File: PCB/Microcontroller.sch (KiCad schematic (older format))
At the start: 25 parts

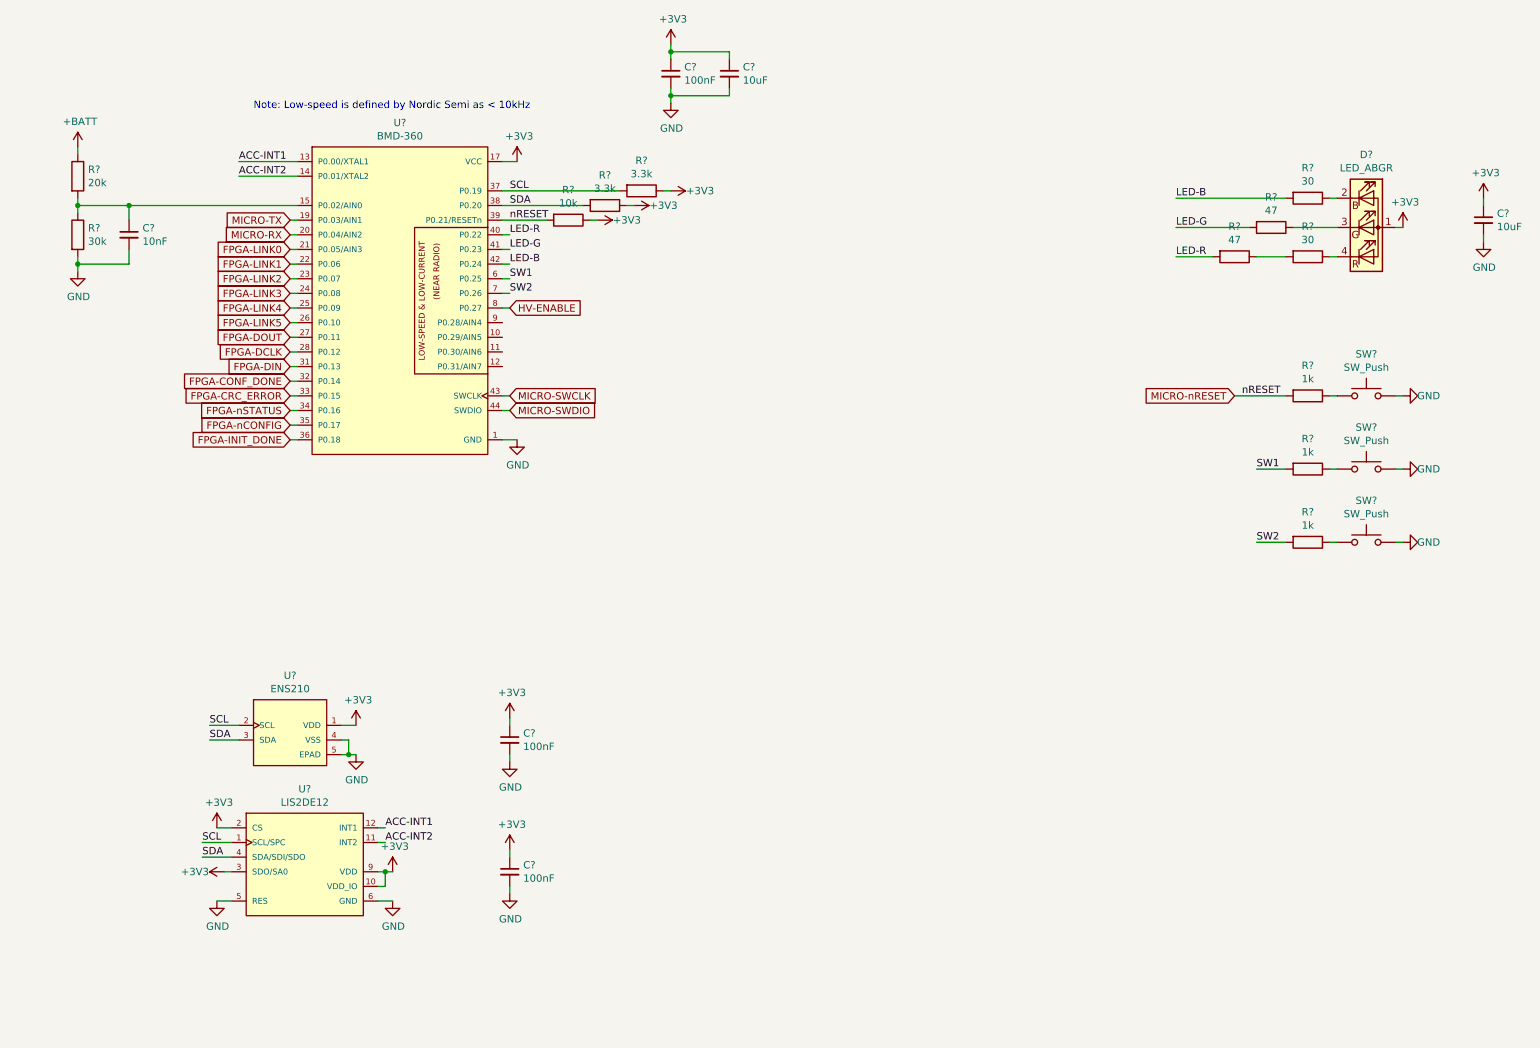
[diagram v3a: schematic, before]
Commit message: Add comparator to monitor 50V supply, add flash memory for storing FPGA config data
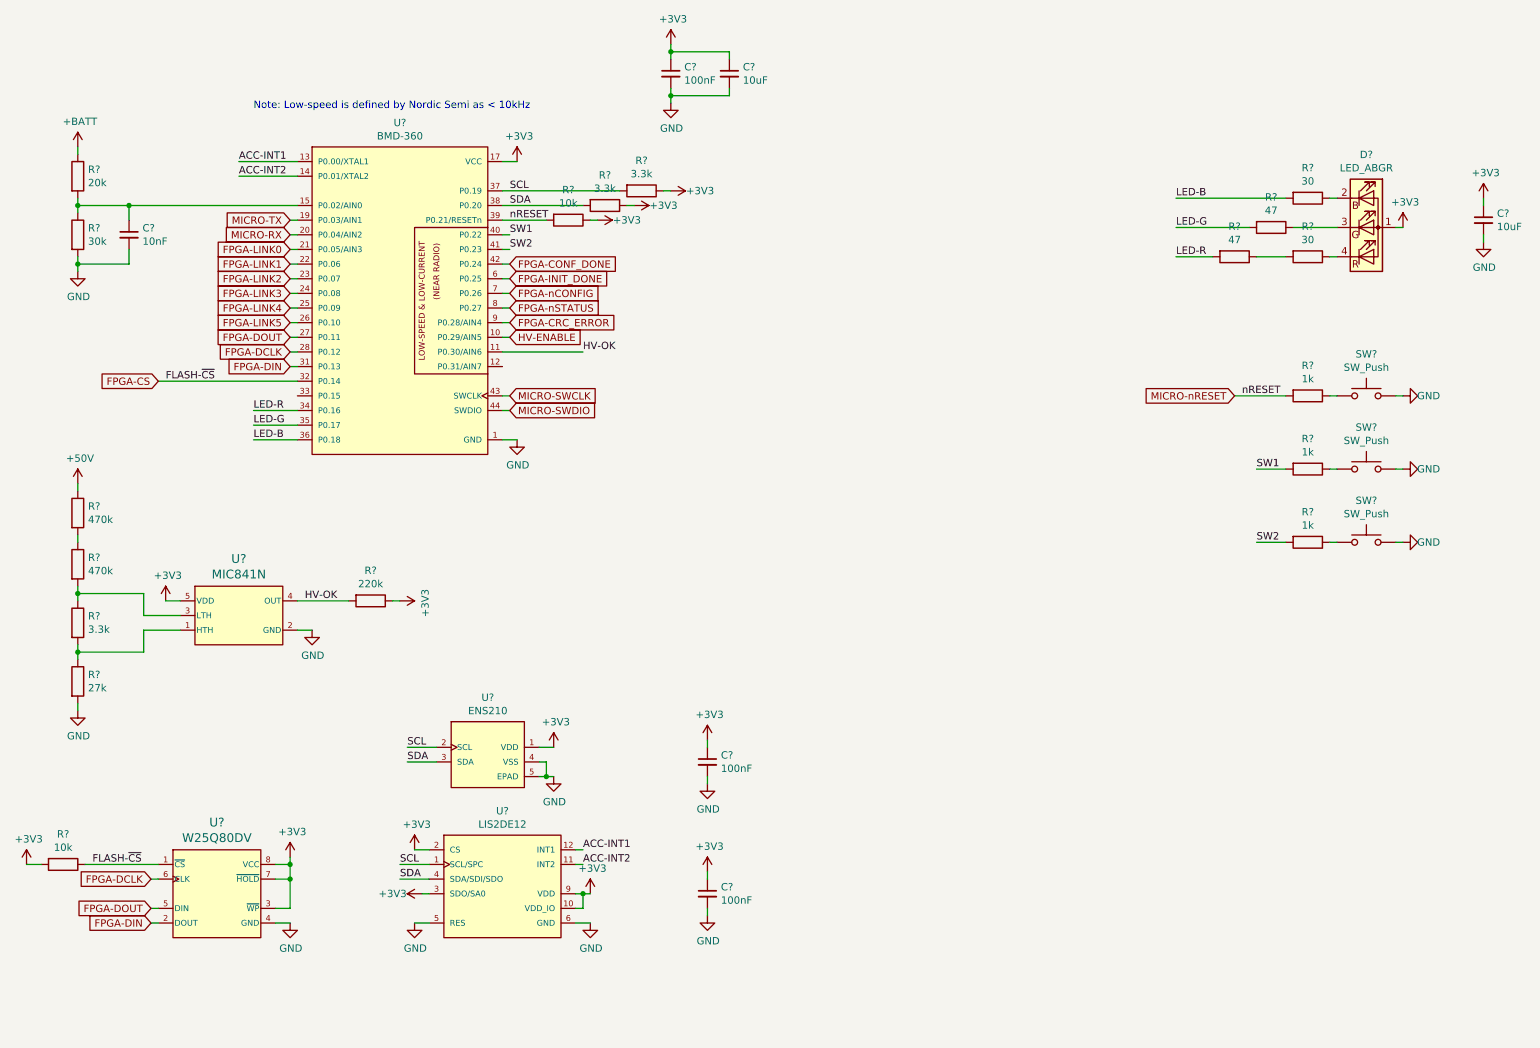
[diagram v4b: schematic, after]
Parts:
- added R?: 3.3k, Resistors_SMD:R_0603_HandSoldering, symbol Device:R
- added R?: 27k, Resistors_SMD:R_0603_HandSoldering, symbol Device:R
- added R? (x2): 470k, Resistors_SMD:R_0603_HandSoldering, symbol Device:R
- added R?: 220k, Resistors_SMD:R_0603_HandSoldering, symbol Device:R
- added R?: 10k, Resistors_SMD:R_0603_HandSoldering, symbol Device:R
- added U?: MIC841N, Parts:SOT353, symbol Parts:MIC841N
- added U?: W25Q80DV, Parts:SOIC8, symbol Parts:W25Q80DV
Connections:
- net +3V3: now also R?.1, R?.2, U?.3 (~WP), U?.5 (VDD), U?.7 (~HOLD), U?.8 (VCC)
- net FPGA-CONF_DONE: now also U?.42 (P0.24); no longer U?.32 (P0.14)
- net FPGA-CRC_ERROR: now also U?.9 (P0.28/AIN4); no longer U?.33 (P0.15)
- net FPGA-DCLK: now also U?.6 (CLK)
- net FPGA-DIN: now also U?.2 (DOUT)
- net FPGA-DOUT: now also U?.5 (DIN)
- net FPGA-INIT_DONE: now also U?.6 (P0.25); no longer U?.36 (P0.18)
- net FPGA-nCONFIG: now also U?.7 (P0.26); no longer U?.35 (P0.17)
- net FPGA-nSTATUS: now also U?.8 (P0.27); no longer U?.34 (P0.16)
- net GND: now also R?.2, U?.2 (GND), U?.4 (GND)
- net HV-ENABLE: now also U?.10 (P0.29/AIN5); no longer U?.8 (P0.27)
- net LED-B: now also U?.36 (P0.18); no longer U?.42 (P0.24)
- net LED-G: now also U?.35 (P0.17); no longer U?.41 (P0.23)
- net LED-R: now also U?.34 (P0.16); no longer U?.40 (P0.22)
- net SW1: now also U?.40 (P0.22); no longer U?.6 (P0.25)
- net SW2: now also U?.41 (P0.23); no longer U?.7 (P0.26)
- net HV-OK: now reaches U?.11 (P0.30/AIN6)
- net HV-OK: now also R?.2, U?.4 (OUT)
- new net: R?.1, R?.2, U?.1 (HTH)
- new net: R?.1, R?.2, U?.3 (LTH)
- new net: R?.1, R?.2
- new net +50V: R?.1
- new net FPGA-CS: R?.1, U?.1 (~CS), U?.32 (P0.14)
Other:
- moved on the sheet: C?, U?

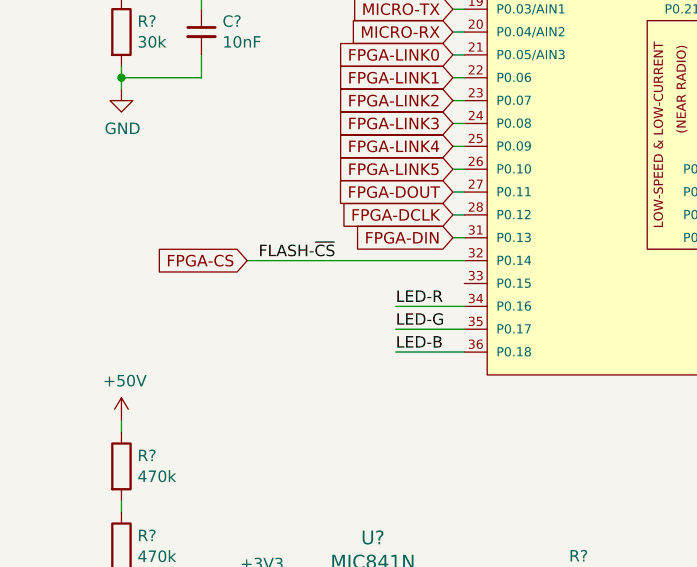
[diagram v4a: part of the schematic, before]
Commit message: Switch to diodes that will waste less transmit power, add amplifier to generate transmit midrail, add enable signal to final amplifier
Enable signal to final amplifier is important, as it will allow us to conserve power when not transmitting. This should help keep the amplifier from overheating.
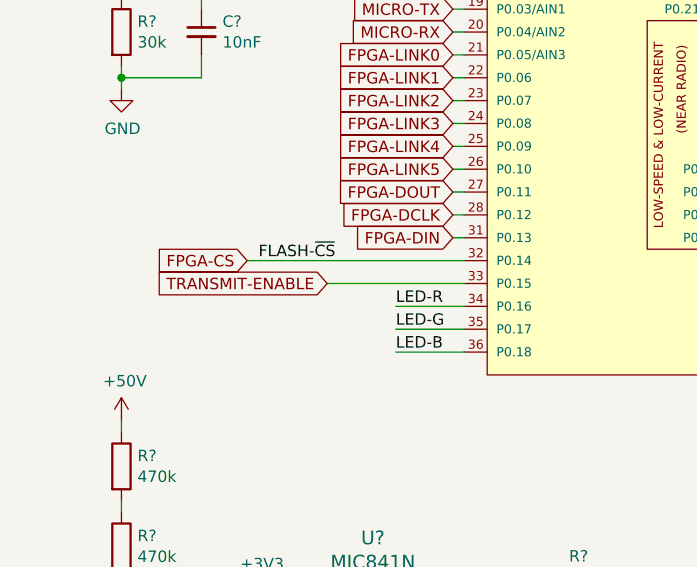
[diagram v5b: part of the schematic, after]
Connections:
- net TRANSMIT-ENABLE: now reaches U?.33 (P0.15)
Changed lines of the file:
@@
 Wire Wire Line
 	1550 6800 1600 6800
+Text GLabel 1950 3300 0    50   Input ~ 0
+TRANSMIT-ENABLE
+Wire Wire Line
+	1950 3300 2550 3300
 $EndSCHEMATC

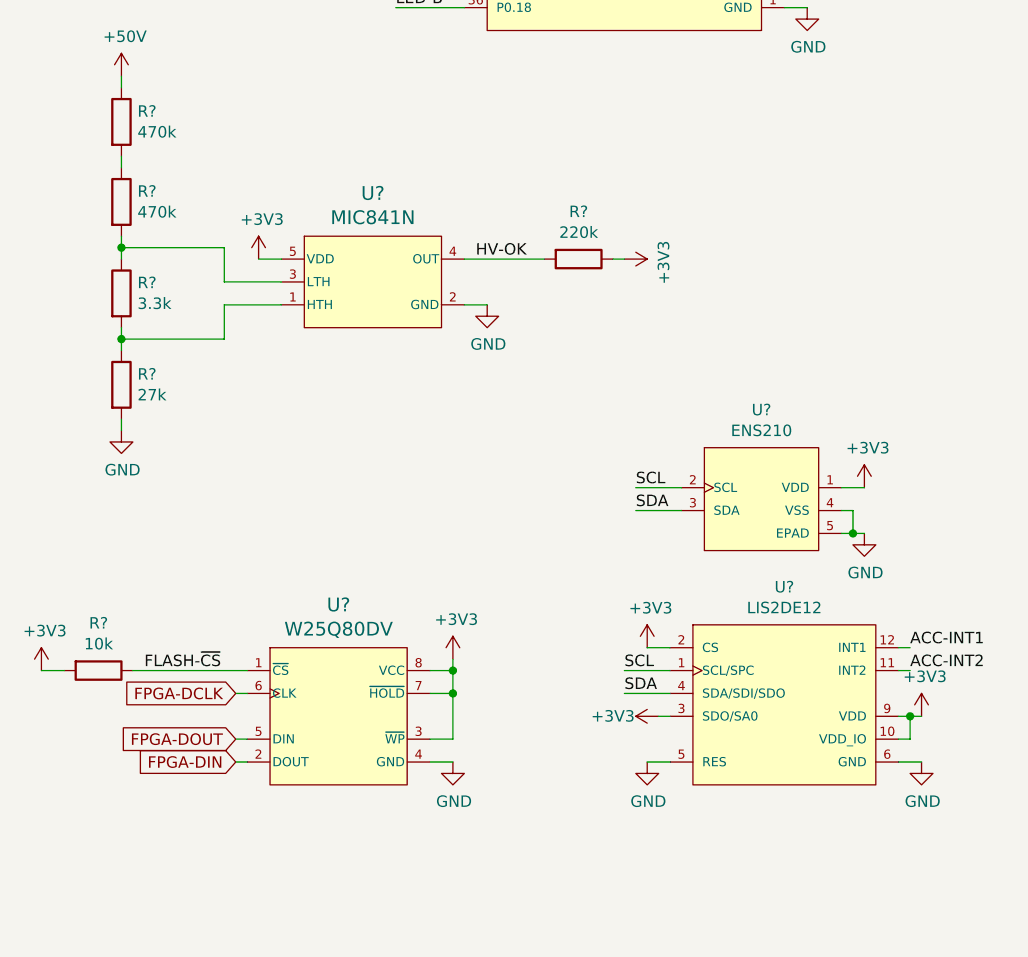
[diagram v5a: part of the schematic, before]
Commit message: Add decoupling capacitors for components without
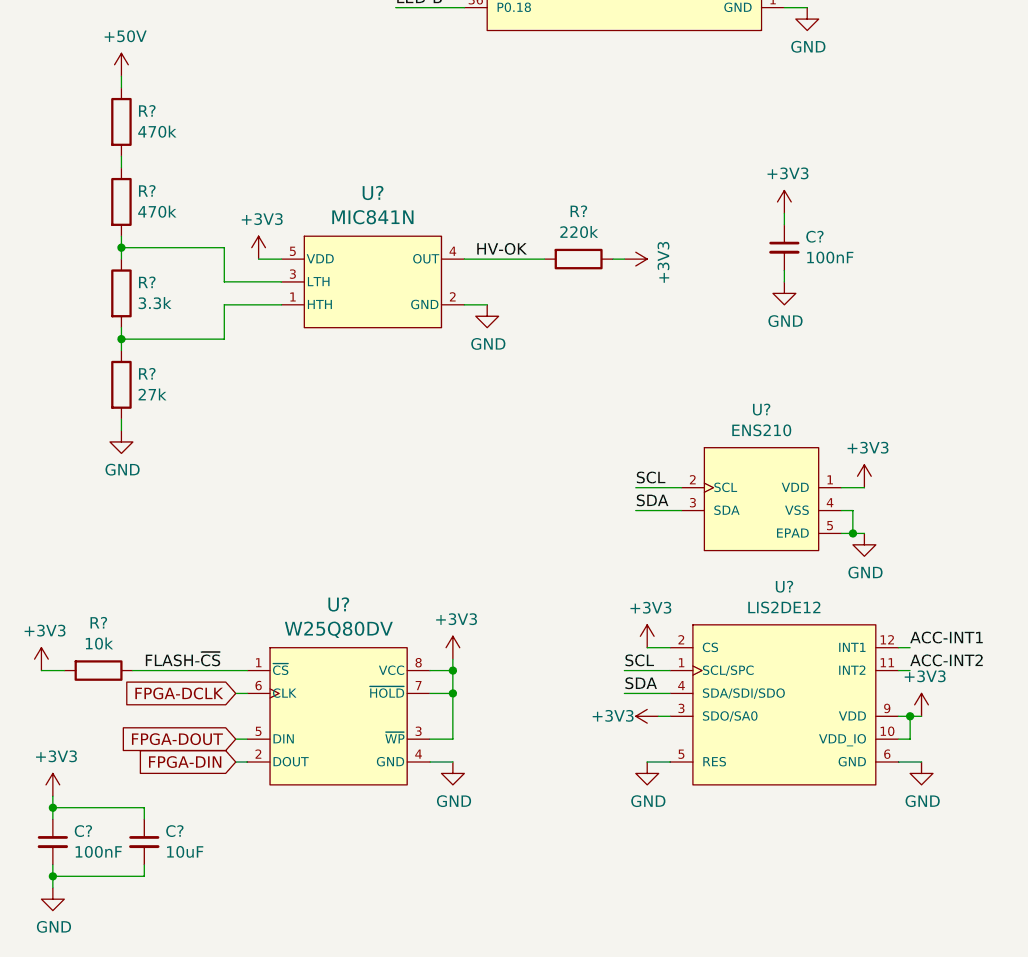
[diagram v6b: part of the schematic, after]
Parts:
- added C? (x2): 100nF, Capacitors_SMD:C_0603_HandSoldering, symbol Device:C_Small
- added C?: 10uF, Capacitors_SMD:C_0805_HandSoldering, symbol Device:C_Small
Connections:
- net +3V3: now also C?.1, C?.1, C?.1
- net GND: now also C?.2, C?.2, C?.2
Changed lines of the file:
@@
 $EndComp
 $Comp
-L power:+3V3 #PWR0125
+L power:+3V3 #PWR?
 U 1 1 5DCF44EC
 P 4050 1700
-F 0 "#PWR0125" H 4050 1550 50  0001 C CNN
+F 0 "#PWR?" H 4050 1550 50  0001 C CNN
 F 1 "+3V3" H 4065 1873 50  0000 C CNN
 F 2 "" H 4050 1700 50  0001 C CNN
@@
 	3950 1700 4050 1700
 $Comp
-L power:GND #PWR0126
+L power:GND #PWR?
 U 1 1 5DCF5A78
 P 4050 3600
-F 0 "#PWR0126" H 4050 3350 50  0001 C CNN
+F 0 "#PWR?" H 4050 3350 50  0001 C CNN
 F 1 "GND" H 4055 3427 50  0000 C CNN
 F 2 "" H 4050 3600 50  0001 C CNN
@@
 	4000 3400 3950 3400
 $Comp
-L power:+3V3 #PWR0127
+L power:+3V3 #PWR?
 U 1 1 5DCF6F82
 P 10100 2150
-F 0 "#PWR0127" H 10100 2000 50  0001 C CNN
+F 0 "#PWR?" H 10100 2000 50  0001 C CNN
 F 1 "+3V3" H 10115 2323 50  0000 C CNN
 F 2 "" H 10100 2150 50  0001 C CNN
@@
 Wire Wire Line
 	1950 3300 2550 3300
+$Comp
+L Device:C_Small C?
+U 1 1 5E3DE021
+P 750 7250
+F 0 "C?" H 842 7296 50  0000 L CNN
+F 1 "100nF" H 842 7205 50  0000 L CNN
+F 2 "Capacitors_SMD:C_0603_HandSoldering" H 750 7250 50  0001 C CNN
+F 3 "https://www.digikey.ca/product-detail/en/w-rth-elektronik/885012206020/732-7939-1-ND/5454566" H 750 7250 50  0001 C CNN
+	1    750  7250
+	1    0    0    -1
+$EndComp
+$Comp
+L power:+3V3 #PWR?
+U 1 1 5E3DE02B
+P 750 7050
+F 0 "#PWR?" H 750 6900 50  0001 C CNN
+F 1 "+3V3" H 765 7223 50  0000 C CNN
+F 2 "" H 750 7050 50  0001 C CNN
+F 3 "" H 750 7050 50  0001 C CNN
+	1    750  7050
+	1    0    0    -1
+$EndComp
+$Comp
+L power:GND #PWR?
+U 1 1 5E3DE035
+P 750 7450
+F 0 "#PWR?" H 750 7200 50  0001 C CNN
+F 1 "GND" H 755 7277 50  0000 C CNN
+F 2 "" H 750 7450 50  0001 C CNN
+F 3 "" H 750 7450 50  0001 C CNN
+	1    750  7450
+	1    0    0    -1
+$EndComp
+Wire Wire Line
+	750  7350 750  7400
+Wire Wire Line
+	750  7050 750  7100
+$Comp
+L Device:C_Small C?
+U 1 1 5E3DE041
+P 1150 7250
+F 0 "C?" H 1242 7296 50  0000 L CNN
+F 1 "10uF" H 1242 7205 50  0000 L CNN
+F 2 "Capacitors_SMD:C_0805_HandSoldering" H 1150 7250 50  0001 C CNN
+F 3 "https://www.digikey.ca/product-detail/en/kemet/C0805C106K8PACTU/399-4925-1-ND/1090920" H 1150 7250 50  0001 C CNN
+	1    1150 7250
+	1    0    0    -1
+$EndComp
+Wire Wire Line
+	750  7100 1150 7100
+Wire Wire Line
+	1150 7100 1150 7150
+Connection ~ 750  7100
+Wire Wire Line
+	750  7100 750  7150
+Wire Wire Line
+	1150 7350 1150 7400
+Wire Wire Line
+	1150 7400 750  7400
+Connection ~ 750  7400
+Wire Wire Line
+	750  7400 750  7450
+Wire Wire Line
+	3950 4500 3950 4550
+Wire Wire Line
+	3950 4750 3950 4800
+$Comp
+L power:GND #PWR?
+U 1 1 5E3E92C6
+P 3950 4800
+F 0 "#PWR?" H 3950 4550 50  0001 C CNN
+F 1 "GND" H 3955 4627 50  0000 C CNN
+F 2 "" H 3950 4800 50  0001 C CNN
+F 3 "" H 3950 4800 50  0001 C CNN
+	1    3950 4800
+	1    0    0    -1
+$EndComp
+$Comp
+L power:+3V3 #PWR?
+U 1 1 5E3E92D0
+P 3950 4500
+F 0 "#PWR?" H 3950 4350 50  0001 C CNN
+F 1 "+3V3" H 3965 4673 50  0000 C CNN
+F 2 "" H 3950 4500 50  0001 C CNN
+F 3 "" H 3950 4500 50  0001 C CNN
+	1    3950 4500
+	1    0    0    -1
+$EndComp
+$Comp
+L Device:C_Small C?
+U 1 1 5E3E92DA
+P 3950 4650
+F 0 "C?" H 4042 4696 50  0000 L CNN
+F 1 "100nF" H 4042 4605 50  0000 L CNN
+F 2 "Capacitors_SMD:C_0603_HandSoldering" H 3950 4650 50  0001 C CNN
+F 3 "https://www.digikey.ca/product-detail/en/w-rth-elektronik/885012206020/732-7939-1-ND/5454566" H 3950 4650 50  0001 C CNN
+	1    3950 4650
+	1    0    0    -1
+$EndComp
 $EndSCHEMATC

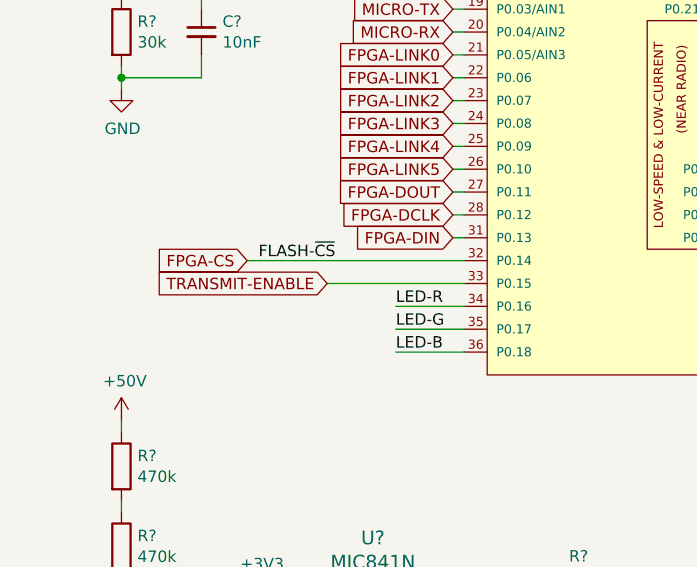
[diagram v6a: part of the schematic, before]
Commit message: Changed transmit-enable to connect to FPGA instead of microcontroller, added 10V linear regulator
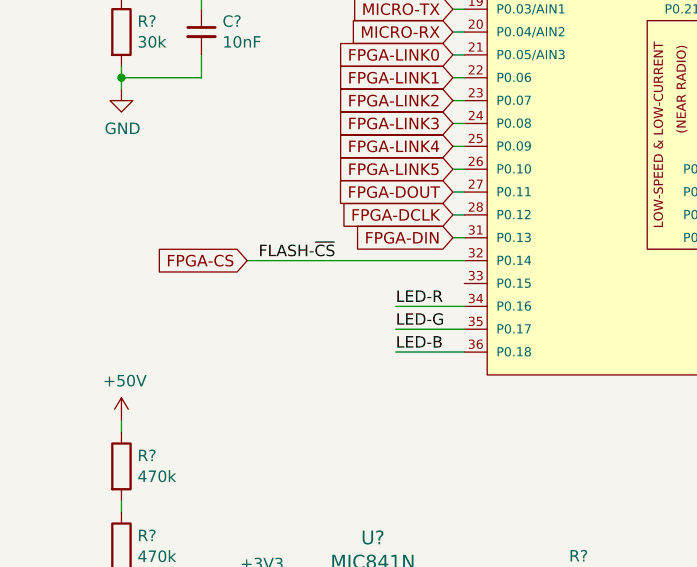
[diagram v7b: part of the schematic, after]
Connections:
- net TRANSMIT-ENABLE: no longer names the net of U?.33 (P0.15)
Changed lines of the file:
@@
 Wire Wire Line
 	1550 6800 1600 6800
-Text GLabel 1950 3300 0    50   Input ~ 0
-TRANSMIT-ENABLE
-Wire Wire Line
-	1950 3300 2550 3300
 $Comp
 L Device:C_Small C?

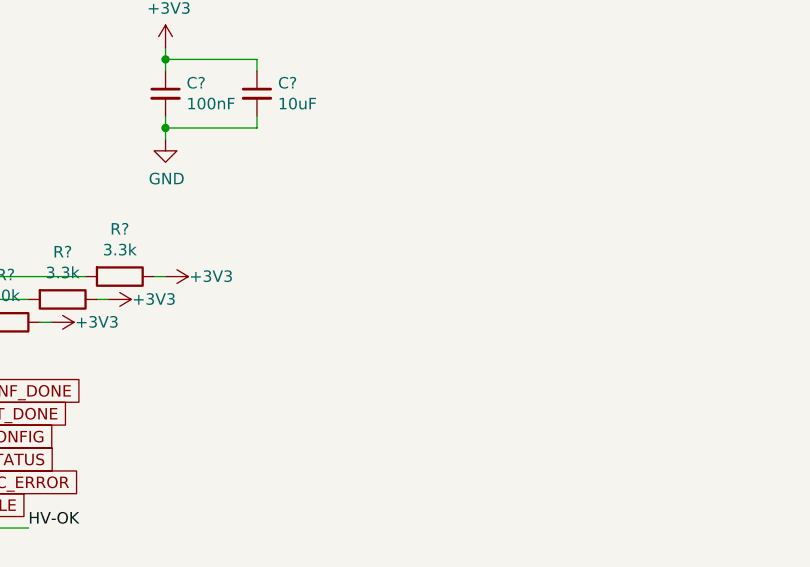
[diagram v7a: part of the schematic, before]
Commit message: Bring additional signals to the connectors sheet for debug access
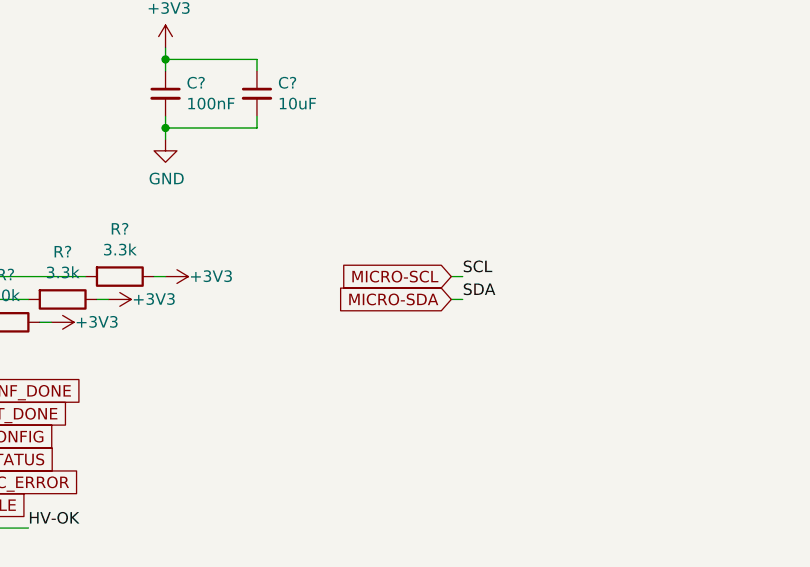
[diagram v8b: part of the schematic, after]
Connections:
- net SCL renamed MICRO-SCL
- net SDA renamed MICRO-SDA
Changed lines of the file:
@@
 	1    0    0    -1
 $EndComp
+Text GLabel 6350 1900 0    50   Input ~ 0
+MICRO-SCL
+Text GLabel 6350 2000 0    50   Input ~ 0
+MICRO-SDA
+Text Label 6400 1900 0    50   ~ 0
+SCL
+Text Label 6400 2000 0    50   ~ 0
+SDA
+Wire Wire Line
+	6350 1900 6400 1900
+Wire Wire Line
+	6350 2000 6400 2000
 $EndSCHEMATC
